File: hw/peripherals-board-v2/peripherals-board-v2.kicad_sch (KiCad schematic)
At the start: 25 parts, among them J1 Power/Motor Screw Terminal, J10 Extra Servo, J11 Conn_02x05_Odd_Even, J2 OLED, J3 BNO055, J4 LiDAR Right, J5 Radio Input, J6 LiDAR Left, J7 LiDAR Front, J8 Motor Encoder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

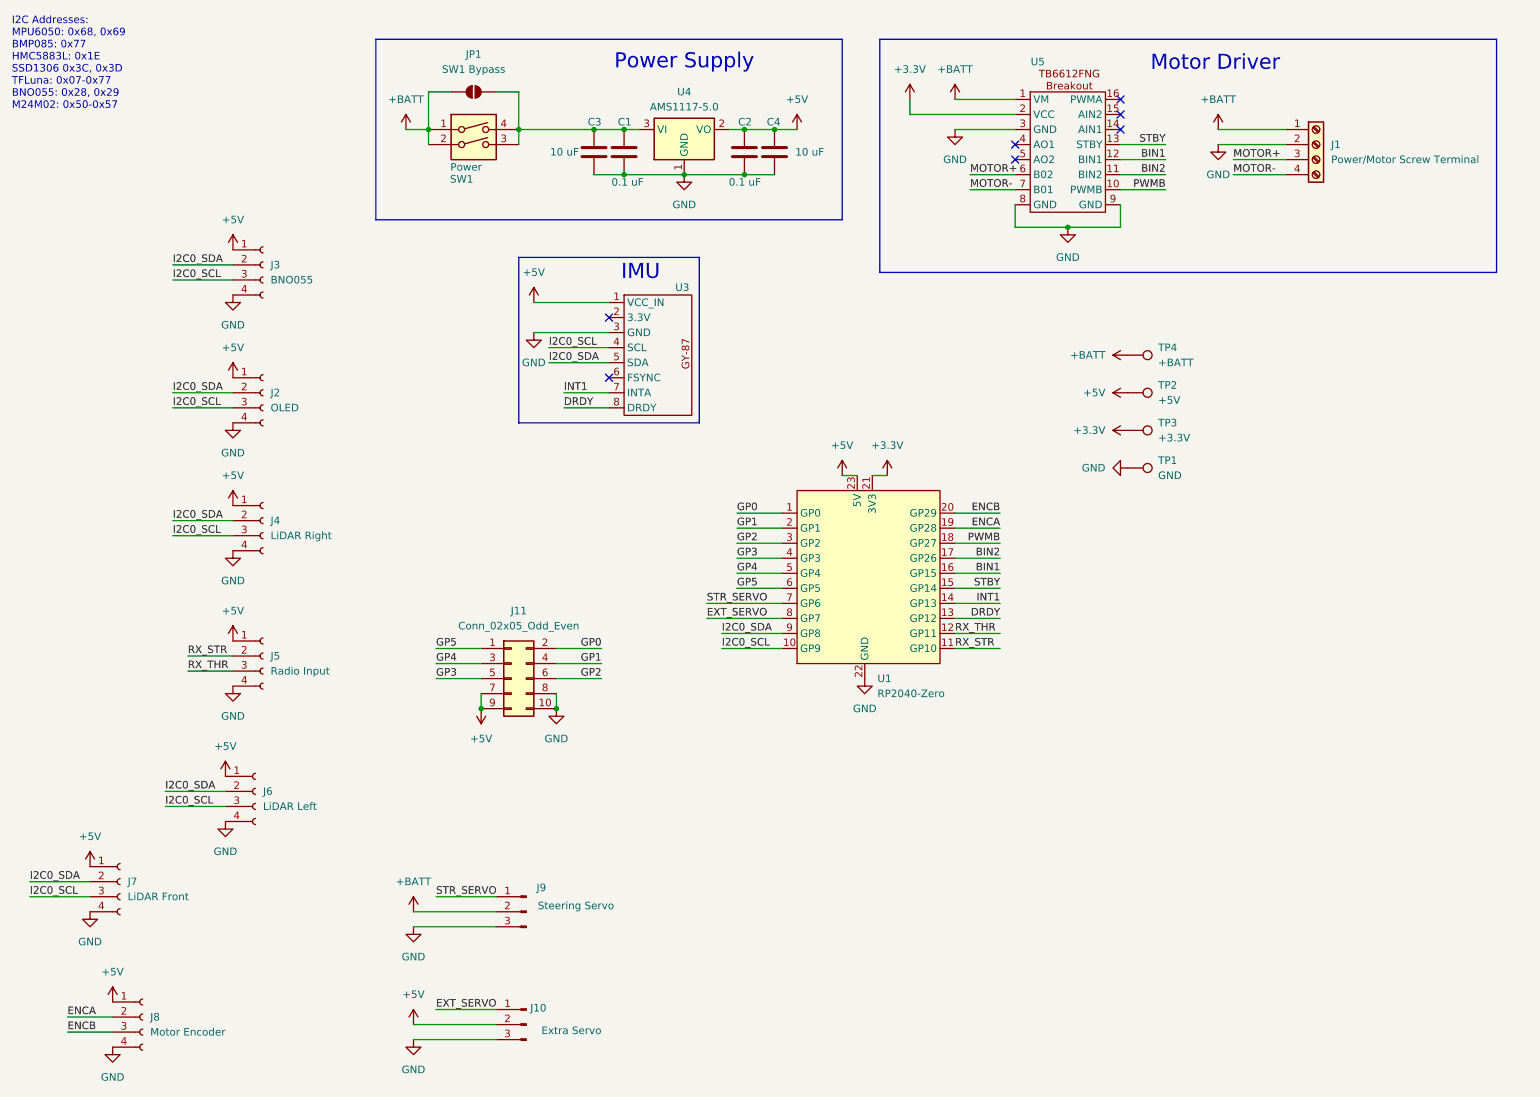
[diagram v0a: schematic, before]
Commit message: Update peripherals board schematic and layout
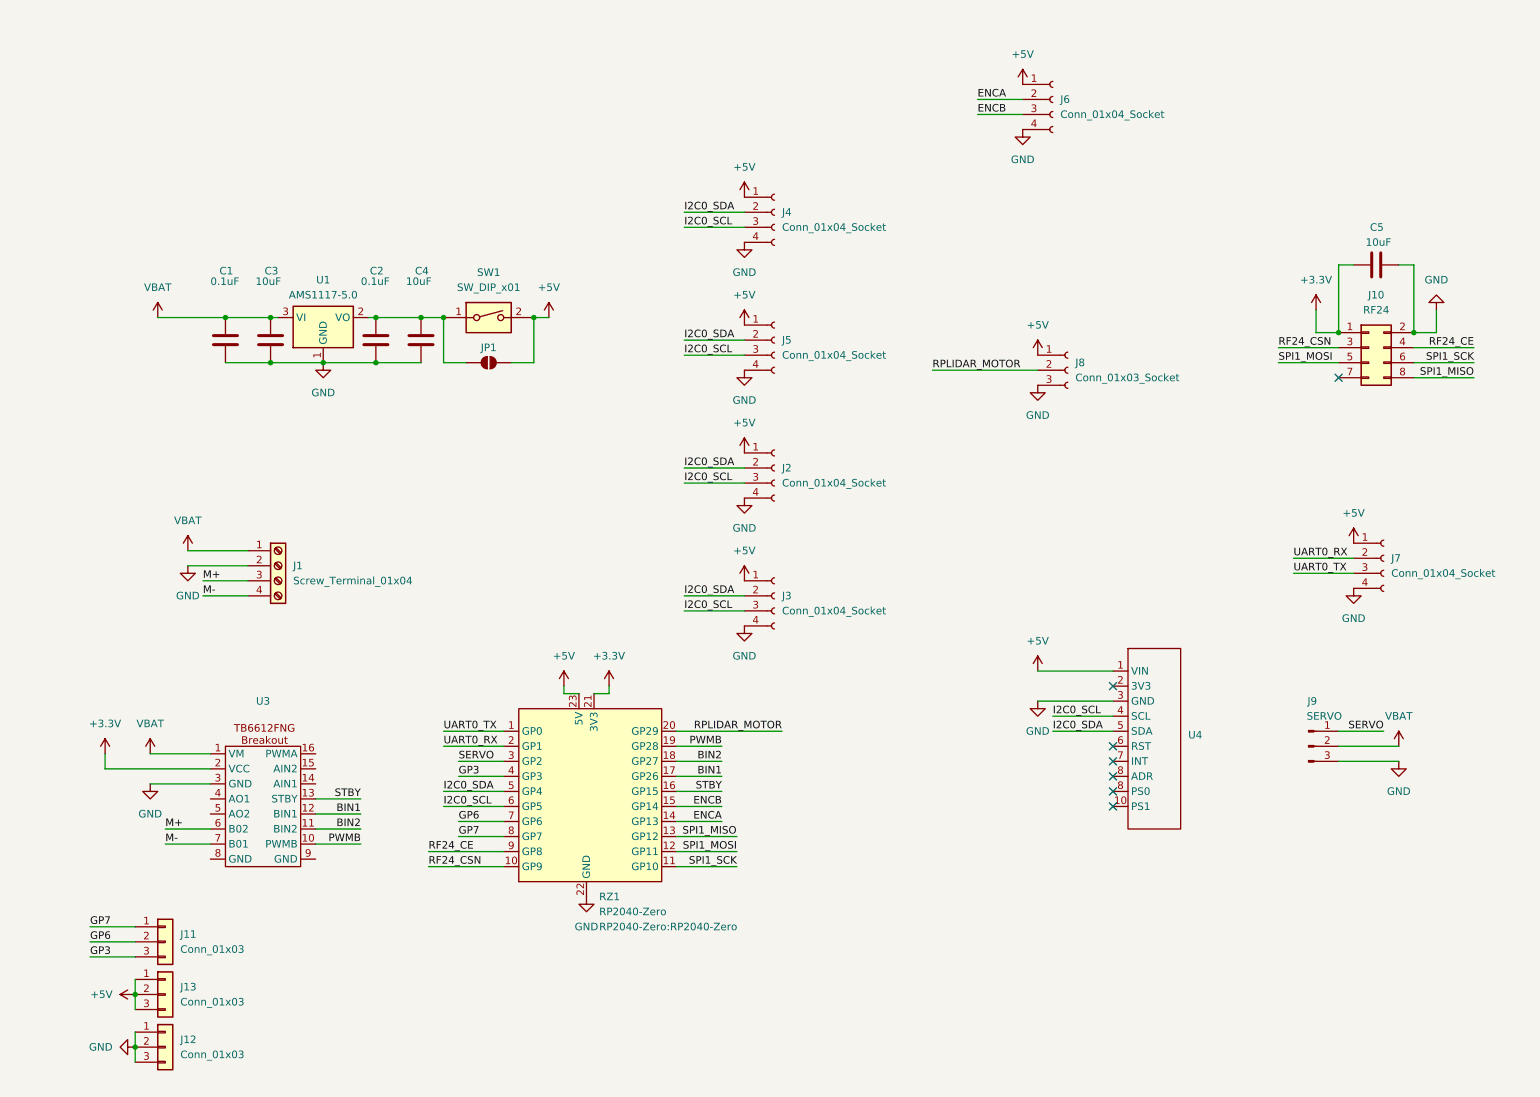
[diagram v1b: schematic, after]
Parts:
- removed J10: Extra Servo, Connector_PinHeader_2.54mm:PinHeader_1x03_P2.54mm_Vertical, symbol Connector:Conn_01x03_Pin
- removed J11: Conn_02x05_Odd_Even, Connector_PinSocket_2.54mm:PinSocket_2x05_P2.54mm_Vertical, symbol Connector_Generic:Conn_02x05_Odd_Even
- removed J8: Motor Encoder, Connector_JST:JST_EH_S4B-EH_1x04_P2.50mm_Horizontal, symbol Connector:Conn_01x04_Socket
- removed SW1: Power, Package_DIP:DIP-4_W7.62mm, symbol Switch:SW_DIP_x02
- removed TP1: GND, TestPoint:TestPoint_Pad_D1.5mm, symbol Connector:TestPoint
- removed TP2: +5V, TestPoint:TestPoint_Pad_D1.5mm, symbol Connector:TestPoint
- removed TP3: +3.3V, TestPoint:TestPoint_Pad_D1.5mm, symbol Connector:TestPoint
- removed TP4: +BATT, TestPoint:TestPoint_Pad_D1.5mm, symbol Connector:TestPoint
- removed U1: RP2040-Zero, RP2040-Zero:RP2040-Zero, symbol rp2040-zero:RP2040-Zero
- removed U3: ~, GY87:GY87, symbol GY87:GY87
- removed U4: AMS1117-5.0, Package_TO_SOT_SMD:SOT-223-3_TabPin2, symbol Regulator_Linear:AMS1117-5.0
- removed U5: ~, TB6612FNG-breakout:TB6612FNG-breakout, symbol TB6612FNG-breakout:TB6612FNG-breakout
- added C5: 10uF, Capacitor_SMD:C_0805_2012Metric_Pad1.18x1.45mm_HandSolder, symbol Device:C
- added J10: RF24, Connector_PinSocket_2.54mm:PinSocket_2x04_P2.54mm_Vertical, symbol Connector_Generic:Conn_02x04_Odd_Even
- added J11, J12, J13: Conn_01x03, Connector_PinSocket_2.54mm:PinSocket_1x03_P2.54mm_Vertical, symbol Connector_Generic:Conn_01x03
- added J8: Conn_01x03_Socket, JST_XH_01x03_Horizontal_NoFlange:JST_XH_01x03_Horizontal_NoFlange, symbol Connector:Conn_01x03_Socket
- added RZ1: RP2040-Zero, RP2040-Zero:RP2040-Zero, symbol rp2040-zero:RP2040-Zero
- added SW1: SW_DIP_x01, Button_Switch_THT:SW_DIP_SPSTx01_Slide_6.7x4.1mm_W7.62mm_P2.54mm_LowProfile, symbol Switch:SW_DIP_x01
- added U1: AMS1117-5.0, Package_TO_SOT_SMD:SOT-223-3_TabPin2, symbol Regulator_Linear:AMS1117-5.0
- added U3: ~, TB6612FNG-breakout:TB6612FNG-breakout, symbol TB6612FNG-breakout:TB6612FNG-breakout
- added U4: ~, BNO055-breakout:BNO055-breakout, symbol BNO055-breakout:BNO055-breakout
- C1, C2: value 0.1 uF -> 0.1uF
- C3, C4: value 10 uF -> 10uF
- J1: value Power/Motor Screw Terminal -> Screw_Terminal_01x04; footprint TerminalBlock_RND:TerminalBlock_RND_205-00047_1x04_P5.00mm_Horizontal -> ScrewTerminal_01x04_P5mm:ScrewTerminal_01x04_P5mm
- J2: value OLED -> Conn_01x04_Socket; footprint Connector_JST:JST_EH_S4B-EH_1x04_P2.50mm_Horizontal -> JST_XH_01x04_Horizontal_NoFlange:JST_XH_01x04_Horizontal_NoFlange
- J3: value BNO055 -> Conn_01x04_Socket; footprint Connector_JST:JST_EH_S4B-EH_1x04_P2.50mm_Horizontal -> JST_XH_01x04_Horizontal_NoFlange:JST_XH_01x04_Horizontal_NoFlange
- J4: value LiDAR Right -> Conn_01x04_Socket; footprint Connector_JST:JST_EH_S4B-EH_1x04_P2.50mm_Horizontal -> JST_XH_01x04_Horizontal_NoFlange:JST_XH_01x04_Horizontal_NoFlange
- J5: value Radio Input -> Conn_01x04_Socket; footprint Connector_JST:JST_EH_S4B-EH_1x04_P2.50mm_Horizontal -> JST_XH_01x04_Horizontal_NoFlange:JST_XH_01x04_Horizontal_NoFlange
- J6: value LiDAR Left -> Conn_01x04_Socket; footprint Connector_JST:JST_EH_S4B-EH_1x04_P2.50mm_Horizontal -> JST_XH_01x04_Horizontal_NoFlange:JST_XH_01x04_Horizontal_NoFlange
- J7: value LiDAR Front -> Conn_01x04_Socket; footprint Connector_JST:JST_EH_S4B-EH_1x04_P2.50mm_Horizontal -> JST_XH_01x04_Horizontal_NoFlange:JST_XH_01x04_Horizontal_NoFlange
- J9: value Steering Servo -> SERVO
- JP1: value SW1 Bypass -> SolderJumper_2_Open; footprint Jumper:SolderJumper-2_P1.3mm_Open_RoundedPad1.0x1.5mm -> Jumper:SolderJumper-2_P1.3mm_Open_TrianglePad1.0x1.5mm
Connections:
- net RX_STR is gone; now on net I2C0_SDA: J5.2 (Pin_2)
- net RX_THR is gone; now on net I2C0_SCL: J5.3 (Pin_3)
- net +3.3V: now also C5.1, J10.1 (Pin_1), RZ1.21 (3V3), U3.2 (VCC)
- net +5V: now also JP1.2 (B), J13.1 (Pin_1), J13.2 (Pin_2), J13.3 (Pin_3), J8.1 (Pin_1), RZ1.23 (5V), SW1.2, U4.1 (VIN); no longer C2.1, C4.1
- net BIN1: now also RZ1.17 (GP26), U3.12 (BIN1)
- net BIN2: now also RZ1.18 (GP27), U3.11 (BIN2)
- net ENCA: now also J6.2 (Pin_2), RZ1.14 (GP13)
- net ENCB: now also J6.3 (Pin_3), RZ1.15 (GP14)
- net GND: now also C5.2, J10.2 (Pin_2), J12.1 (Pin_1), J12.2 (Pin_2), J12.3 (Pin_3), J8.3 (Pin_3), RZ1.22 (GND), U1.1 (GND), U3.3 (GND), U4.3 (GND)
- net GP3: now also J11.3 (Pin_3), RZ1.4 (GP3)
- net I2C0_SCL: now also RZ1.6 (GP5), U4.4 (SCL); no longer J6.3 (Pin_3), J7.3 (Pin_3)
- net I2C0_SDA: now also RZ1.5 (GP4), U4.5 (SDA); no longer J6.2 (Pin_2), J7.2 (Pin_2)
- net PWMB: now also RZ1.19 (GP28), U3.10 (PWMB)
- net STBY: now also RZ1.16 (GP15), U3.13 (STBY)
- net VBAT: now reaches C1.1, C3.1
- net VBAT: now also J1.1 (Pin_1), J9.2 (Pin_2), U1.3 (VI), U3.1 (VM); no longer JP1.2 (B)
- removed net +BATT: J1.1 (Pin_1), J9.2 (Pin_2), JP1.1 (A)
- net MOTOR+ renamed M+
- net M+: now also U3.6 (B02)
- net MOTOR- renamed M-
- net M-: now also U3.7 (B01)
- net STR_SERVO renamed SERVO
- net SERVO: now also RZ1.3 (GP2)
- new net: C2.1, C4.1, JP1.1 (A), SW1.1, U1.2 (VO)
- new net GP6: J11.2 (Pin_2), RZ1.7 (GP6)
- new net GP7: J11.1 (Pin_1), RZ1.8 (GP7)
- new net RF24_CE: J10.4 (Pin_4), RZ1.9 (GP8)
- new net RF24_CSN: J10.3 (Pin_3), RZ1.10 (GP9)
- new net RPLIDAR_MOTOR: J8.2 (Pin_2), RZ1.20 (GP29)
- new net SPI1_MISO: J10.8 (Pin_8), RZ1.13 (GP12)
- new net SPI1_MOSI: J10.5 (Pin_5), RZ1.12 (GP11)
- new net SPI1_SCK: J10.6 (Pin_6), RZ1.11 (GP10)
- new net UART0_RX: J7.2 (Pin_2), RZ1.2 (GP1)
- new net UART0_TX: J7.3 (Pin_3), RZ1.1 (GP0)
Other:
- note removed: "I2C Addresses: MPU6050: 0x68, 0x69 BMP085: 0x77 HMC5883L: 0x1E SSD1306 0x3C, 0x3D TFLuna: 0x07-0x77 BNO055: 0x28, 0x29 M24M02: 0x50-0x57"
- note removed: "IMU"
- note removed: "Motor Driver"
- note removed: "Power Supply"
